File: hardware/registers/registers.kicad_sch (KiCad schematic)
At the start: 37 parts, among them J1 Conn_Reg, J2 Conn_Reg, J3 Conn_01x20, J4 Conn_Power, J5 Conn_01x10, J6 Conn_01x10, U1 74LVC1G19, U2 74LVC1G19, U3 74LVC1G19, U4 74LVC1G86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

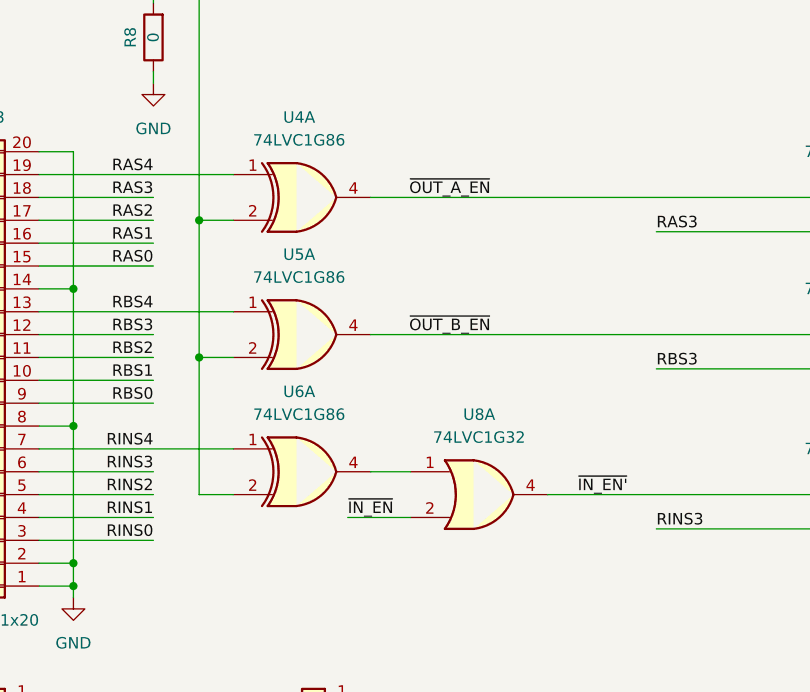
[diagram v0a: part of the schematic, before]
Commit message: Update all to Kicad 6
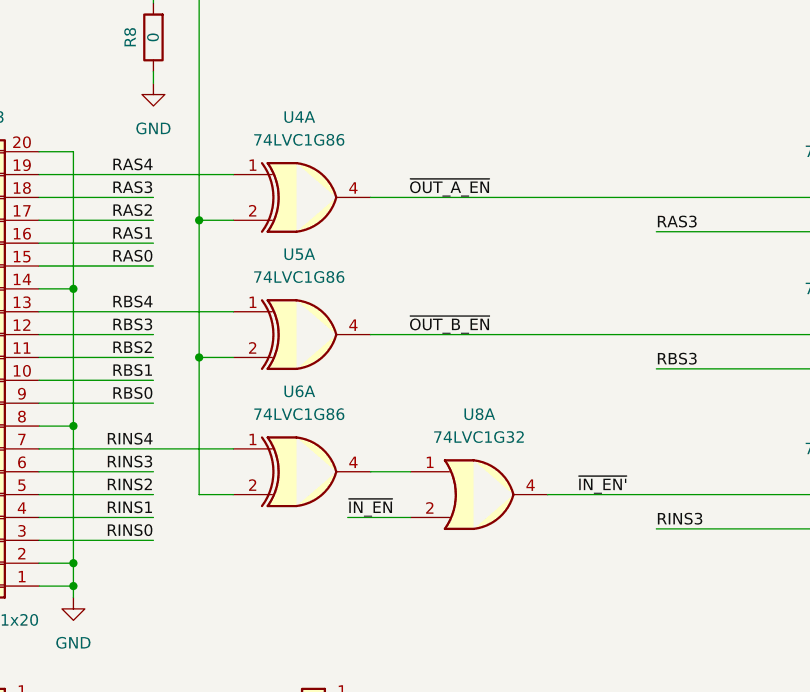
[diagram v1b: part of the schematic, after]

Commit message: Updated schematics and pcbs
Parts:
- added C10: 100n, Capacitor_SMD:C_0805_2012Metric_Pad1.18x1.45mm_HandSolder, symbol Device:C
- added U9: 74LVC1G04, Package_TO_SOT_SMD:SOT-23-5_HandSoldering, symbol riscv-serial:74LVC1G04
- J3: value Conn_01x20 -> Conn_Reg_Sel; symbol Connector_Generic:Conn_01x20 -> riscv-serial:Conn_Reg_Sel
- J5, J6: value Conn_01x10 -> Conn_Reg_Data; symbol Connector_Generic:Conn_01x10 -> riscv-serial:Conn_Reg_Data
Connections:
- net GND: now also C10.2, U9.3 (GND)
- net RESET: now also U9.4; no longer J5.4 (Pin_4), J6.4 (Pin_4)
- net VCC: now also C10.1, U9.5 (VCC)
- new net ~{RESET}: J5.4 (~{RESET}), J6.4 (~{RESET}), U9.2
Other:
- moved on the sheet: C1, C2, C3, C4, C5, C6, C9, U1B, U2B, U3B, U4B, U5B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
